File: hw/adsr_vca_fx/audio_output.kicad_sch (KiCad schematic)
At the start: 16 parts, among them J6 Conn_01x02, J7 Conn_01x02, U4 TL972, U6 TL972

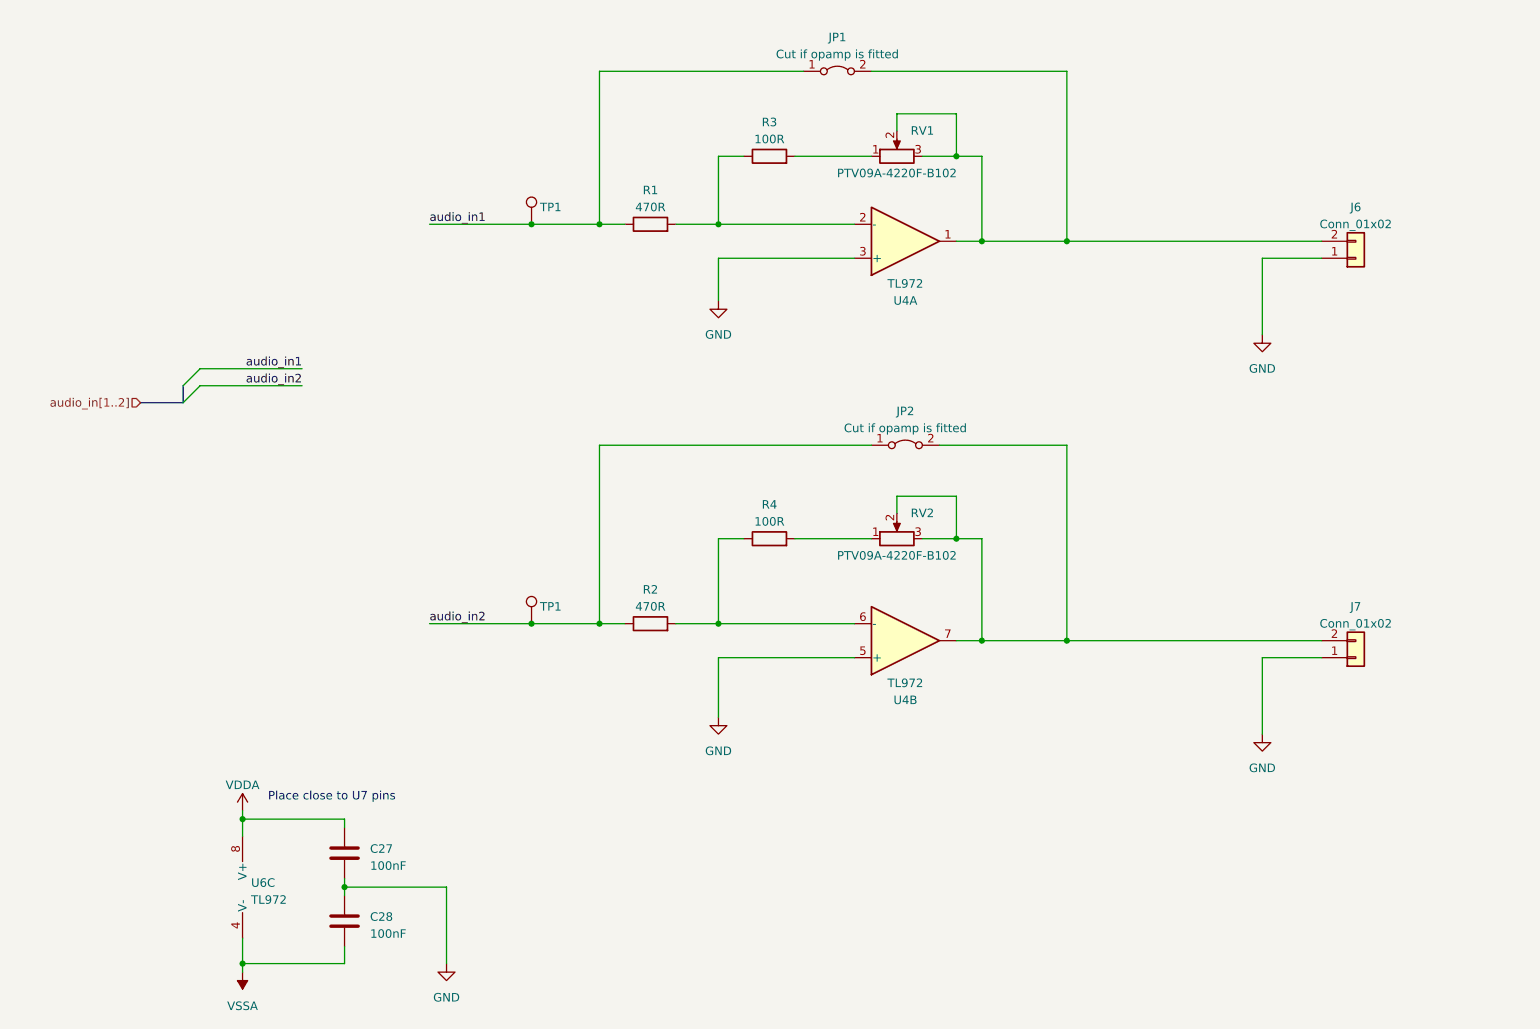
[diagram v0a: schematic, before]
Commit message: modified design into normal/inverted envlope
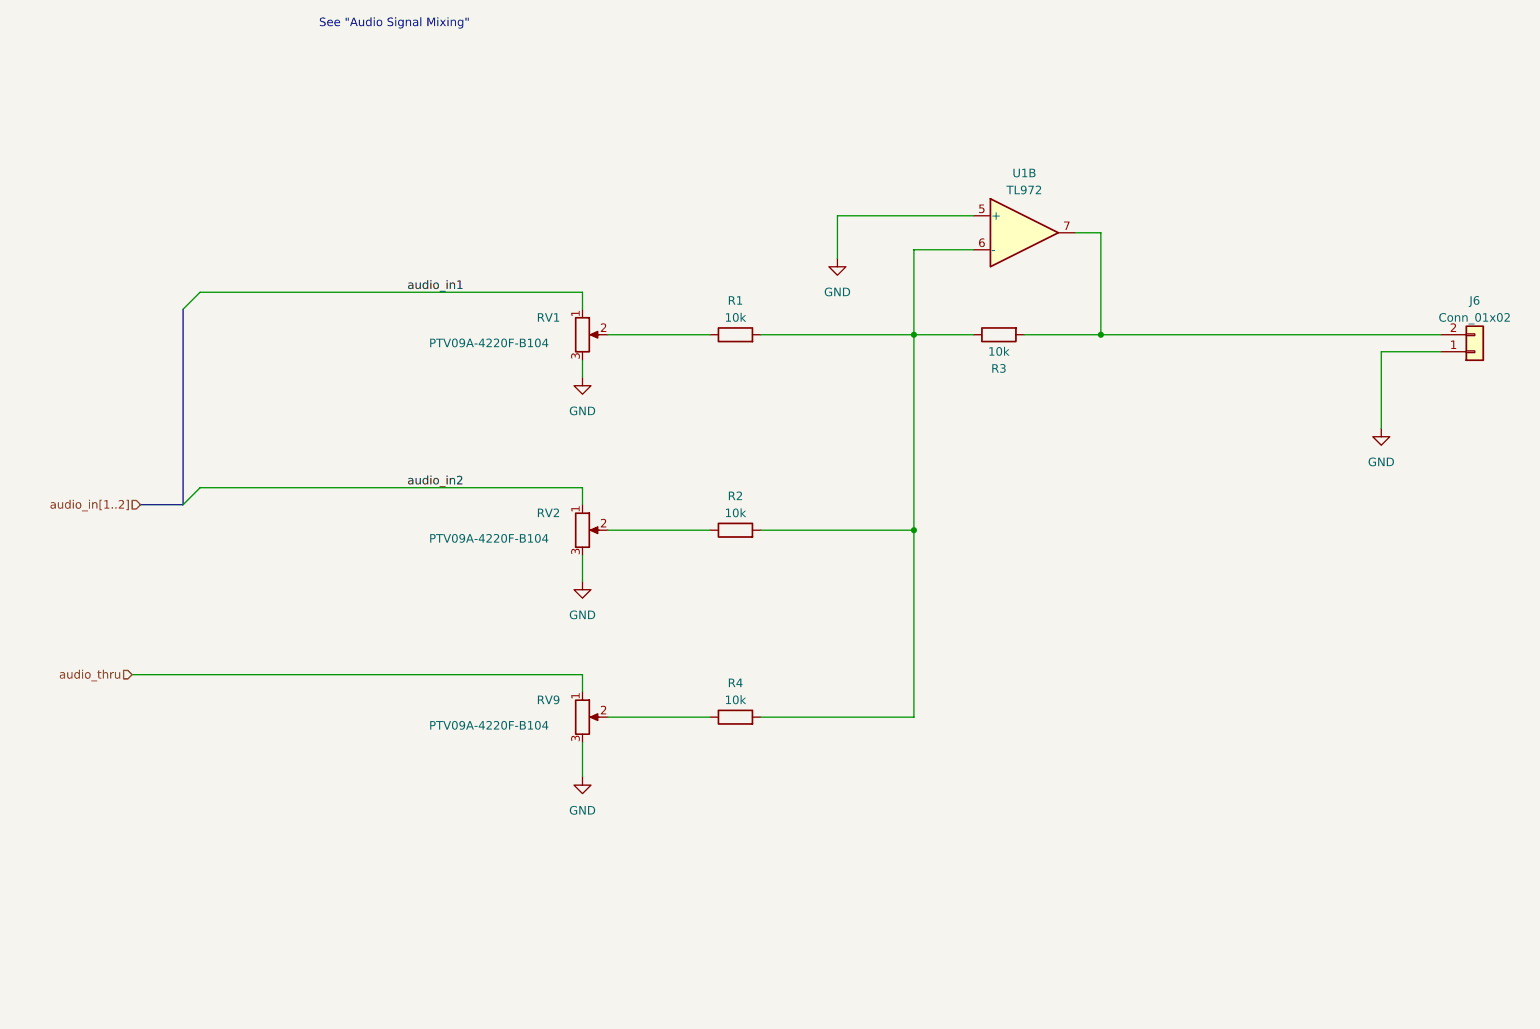
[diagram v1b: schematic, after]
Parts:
- removed C27, C28: 100nF, Capacitor_SMD:C_0805_2012Metric_Pad1.18x1.45mm_HandSolder, symbol Device:C
- removed J7: Conn_01x02, Connector_PinHeader_2.54mm:PinHeader_1x02_P2.54mm_Vertical, symbol Connector_Generic:Conn_01x02
- removed JP1, JP2: Jumper_2_Bridged, Resistor_SMD:R_0805_2012Metric_Pad1.20x1.40mm_HandSolder, symbol Jumper:Jumper_2_Bridged
- removed TP1 (x2): TestPoint, TestPoint:TestPoint_Pad_1.0x1.0mm, symbol Connector:TestPoint
- removed unit 2 of U4
- removed U6: TL972, Package_SO:SOIC-8_3.9x4.9mm_P1.27mm, symbol Amplifier_Operational:TL072
- added RV9: PTV09A-4220F-B104, Potentiometer_THT:Potentiometer_Alpha_RD901F-40-00D_Single_Vertical, symbol Device:R_Potentiometer
- R1, R2: value 470R -> 10k
- R3, R4: value 100R -> 10k
- RV1, RV2: value PTV09A-4220F-B102 -> PTV09A-4220F-B104
- renumbered U4 to U1
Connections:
- net GND: now also RV1.3, RV2.3, U1.5 (+), RV9.3; no longer U1.3 (+)
- net audio_in1: now also RV1.1; no longer R1.1
- net audio_in2: now also RV2.1; no longer R2.1
- net at RV2.2: now also R2.1; no longer RV2.3
- net at R1.2, R3.1: now also R2.2, R4.2, U1.6 (-); no longer U1.2 (-)
- net at R3.2: now also J6.2 (Pin_2), U1.7; no longer RV1.1
- net at R4.1: now also RV9.2; no longer R2.2
- new net: R1.1, RV1.2
- new net audio_thru: RV9.1
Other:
- note added: "See "Audio Signal Mixing""
- note removed: "Place close to U7 pins"
- moved on the sheet: J6, R3, RV1, U1B

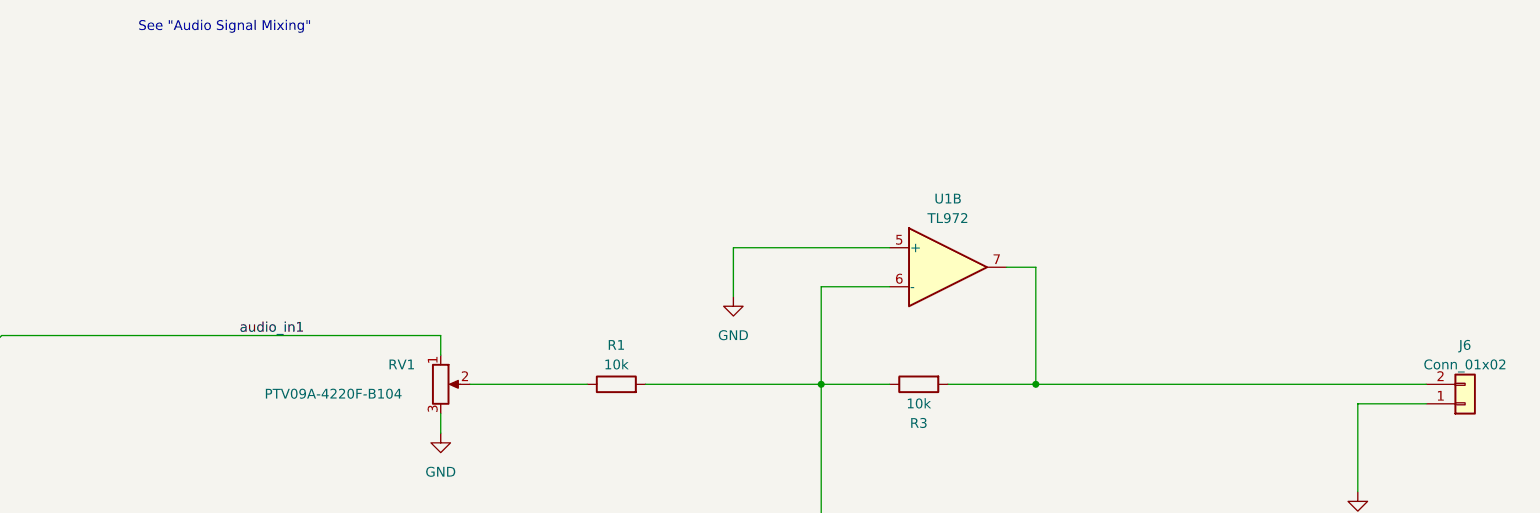
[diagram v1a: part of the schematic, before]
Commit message: updated text labels
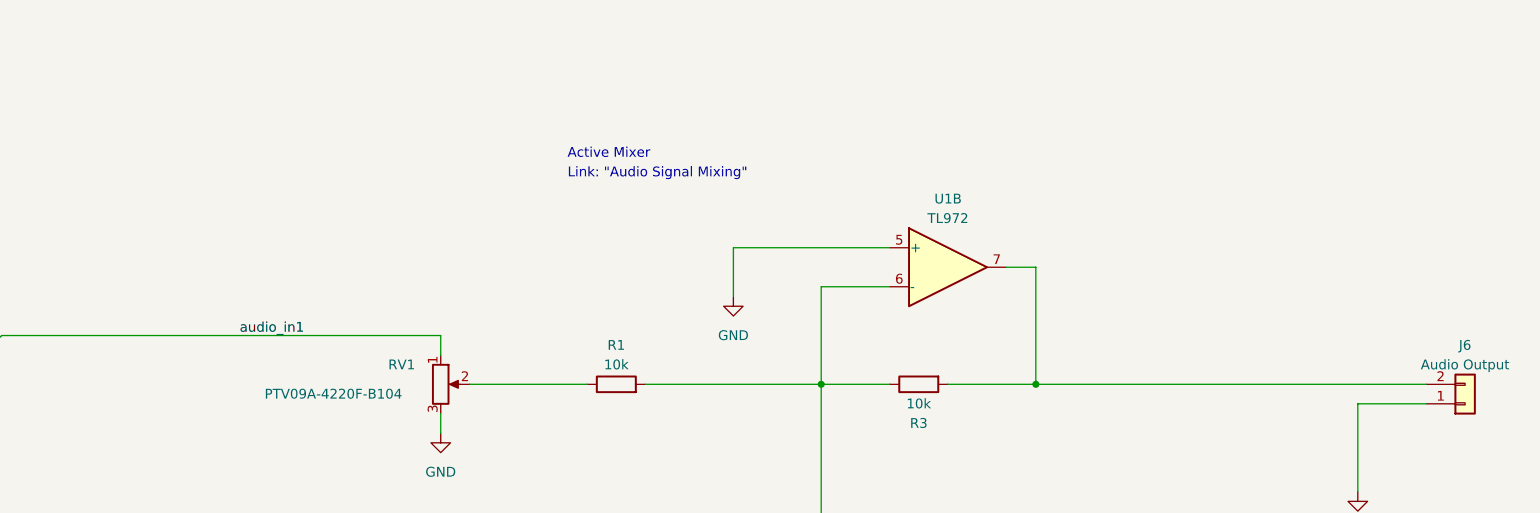
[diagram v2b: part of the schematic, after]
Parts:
- J6: value Conn_01x02 -> Audio Output
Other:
- note added: "Active Mixer"
- note added: "Link: "Audio Signal Mixing""
- note removed: "See "Audio Signal Mixing""
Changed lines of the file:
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@@
     (stroke (width 0) (type default))
   )
-  (text "See \"Audio Signal Mixing\"" (at 81.28 27.94 0)
+  (text "Link: \"Audio Signal Mixing\"" (at 137.16 46.99 0)
     (effects (font (size 1.27 1.27)) (justify left bottom) (href "https://sound-au.com/articles/audio-mixing.htm#s3"))
+  )
+  (text "Active Mixer" (at 137.16 44.45 0)
+    (effects (font (size 1.27 1.27)) (justify left bottom))
   )
   (label "audio_in1" (at 102.87 67.31 180) (fields_autoplaced)
@@
       (effects (font (size 1.27 1.27)))
     )
-    (property "Value" "Conn_01x02" (at 254 71.12 0)
-      (effects (font (size 1.27 1.27)))
-    )
+    (property "Value" "Audio Output" (at 254 71.12 0)
+      (effects (font (size 1.27 1.27)))
+    )

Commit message: first draft layout
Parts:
- renumbered J6 to J5, R1 to R2, R2 to R3, R3 to R5, RV1 to RV2, RV2 to RV3, RV9 to RV4
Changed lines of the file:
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@@
   (symbol (lib_id "Device:R") (at 143.51 102.87 90) (unit 1)
     (in_bom yes) (on_board yes) (dnp no) (fields_autoplaced)
-    (property "Reference" "R2" (at 143.51 97.79 90)
+    (property "Reference" "R3" (at 143.51 97.79 90)
       (effects (font (size 1.27 1.27)))
     )
@@
       (project "adsr_vca_fx"
         (path "/2c7cc946-dcca-4ffb-b6a0-bf0c9ddb491b/8aff0c69-c651-470d-bd06-2b6725b28795"
+          (reference "R3") (unit 1)
+        )
+      )
+    )
+  )
+  (symbol (lib_id "Device:R") (at 143.51 73.66 90) (unit 1)
+    (in_bom yes) (on_board yes) (dnp no) (fields_autoplaced)
+    (property "Reference" "R2" (at 143.51 68.58 90)
+      (effects (font (size 1.27 1.27)))
+    )
+    (property "Value" "10k" (at 143.51 71.12 90)
+      (effects (font (size 1.27 1.27)))
+    )
+    (property "Footprint" "Resistor_SMD:R_0805_2012Metric_Pad1.20x1.40mm_HandSolder" (at 143.51 75.438 90)
+      (effects (font (size 1.27 1.27)) hide)
+    )
+    (property "Datasheet" "~" (at 143.51 73.66 0)
+      (effects (font (size 1.27 1.27)) hide)
+    )
+    (pin "1")
+    (pin "2")
+    (instances
+      (project "adsr_vca_fx"
+        (path "/2c7cc946-dcca-4ffb-b6a0-bf0c9ddb491b/8aff0c69-c651-470d-bd06-2b6725b28795"
           (reference "R2") (unit 1)
-        )
-      )
-    )
-  )
-  (symbol (lib_id "Device:R") (at 143.51 73.66 90) (unit 1)
-    (in_bom yes) (on_board yes) (dnp no) (fields_autoplaced)
-    (property "Reference" "R1" (at 143.51 68.58 90)
-      (effects (font (size 1.27 1.27)))
-    )
-    (property "Value" "10k" (at 143.51 71.12 90)
-      (effects (font (size 1.27 1.27)))
-    )
-    (property "Footprint" "Resistor_SMD:R_0805_2012Metric_Pad1.20x1.40mm_HandSolder" (at 143.51 75.438 90)
-      (effects (font (size 1.27 1.27)) hide)
-    )
-    (property "Datasheet" "~" (at 143.51 73.66 0)
-      (effects (font (size 1.27 1.27)) hide)
-    )
-    (pin "1")
-    (pin "2")
-    (instances
-      (project "adsr_vca_fx"
-        (path "/2c7cc946-dcca-4ffb-b6a0-bf0c9ddb491b/8aff0c69-c651-470d-bd06-2b6725b28795"
-          (reference "R1") (unit 1)
         )
       )
@@
   (symbol (lib_id "Device:R_Potentiometer") (at 120.65 130.81 0) (unit 1)
     (in_bom yes) (on_board yes) (dnp no)
-    (property "Reference" "RV9" (at 115.57 128.27 0)
+    (property "Reference" "RV4" (at 115.57 128.27 0)
       (effects (font (size 1.27 1.27)))
     )
@@
       (project "adsr_vca_fx"
         (path "/2c7cc946-dcca-4ffb-b6a0-bf0c9ddb491b/8aff0c69-c651-470d-bd06-2b6725b28795"
-          (reference "RV9") (unit 1)
+          (reference "RV4") (unit 1)
         )
       )
@@
   (symbol (lib_id "Device:R") (at 182.88 73.66 90) (mirror x) (unit 1)
     (in_bom yes) (on_board yes) (dnp no) (fields_autoplaced)
-    (property "Reference" "R3" (at 182.88 78.74 90)
+    (property "Reference" "R5" (at 182.88 78.74 90)
       (effects (font (size 1.27 1.27)))
     )
@@
       (project "adsr_vca_fx"
         (path "/2c7cc946-dcca-4ffb-b6a0-bf0c9ddb491b/8aff0c69-c651-470d-bd06-2b6725b28795"
-          (reference "R3") (unit 1)
+          (reference "R5") (unit 1)
         )
       )
@@
   (symbol (lib_id "Device:R_Potentiometer") (at 120.65 73.66 0) (unit 1)
     (in_bom yes) (on_board yes) (dnp no)
-    (property "Reference" "RV1" (at 115.57 71.12 0)
+    (property "Reference" "RV2" (at 115.57 71.12 0)
       (effects (font (size 1.27 1.27)))
     )
@@
       (project "adsr_vca_fx"
         (path "/2c7cc946-dcca-4ffb-b6a0-bf0c9ddb491b/8aff0c69-c651-470d-bd06-2b6725b28795"
-          (reference "RV1") (unit 1)
+          (reference "RV2") (unit 1)
         )
       )
@@
   (symbol (lib_id "power:GND") (at 240.03 87.63 0) (unit 1)
     (in_bom yes) (on_board yes) (dnp no) (fields_autoplaced)
-    (property "Reference" "#PWR025" (at 240.03 93.98 0)
+    (property "Reference" "#PWR022" (at 240.03 93.98 0)
       (effects (font (size 1.27 1.27)) hide)
     )
@@
       (project "adsr_vca_fx"
         (path "/2c7cc946-dcca-4ffb-b6a0-bf0c9ddb491b/8aff0c69-c651-470d-bd06-2b6725b28795"
-          (reference "#PWR025") (unit 1)
+          (reference "#PWR022") (unit 1)
         )
       )
@@
   (symbol (lib_id "power:GND") (at 120.65 139.7 0) (unit 1)
     (in_bom yes) (on_board yes) (dnp no) (fields_autoplaced)
-    (property "Reference" "#PWR026" (at 120.65 146.05 0)
+    (property "Reference" "#PWR020" (at 120.65 146.05 0)
       (effects (font (size 1.27 1.27)) hide)
     )
@@
       (project "adsr_vca_fx"
         (path "/2c7cc946-dcca-4ffb-b6a0-bf0c9ddb491b/8aff0c69-c651-470d-bd06-2b6725b28795"
-          (reference "#PWR026") (unit 1)
+          (reference "#PWR020") (unit 1)
         )
       )
@@
   (symbol (lib_id "power:GND") (at 120.65 80.01 0) (unit 1)
     (in_bom yes) (on_board yes) (dnp no) (fields_autoplaced)
-    (property "Reference" "#PWR019" (at 120.65 86.36 0)
+    (property "Reference" "#PWR018" (at 120.65 86.36 0)
       (effects (font (size 1.27 1.27)) hide)
     )
@@
       (project "adsr_vca_fx"
         (path "/2c7cc946-dcca-4ffb-b6a0-bf0c9ddb491b/8aff0c69-c651-470d-bd06-2b6725b28795"
+          (reference "#PWR018") (unit 1)
+        )
+      )
+    )
+  )
+  (symbol (lib_id "power:GND") (at 158.75 62.23 0) (unit 1)
+    (in_bom yes) (on_board yes) (dnp no) (fields_autoplaced)
+    (property "Reference" "#PWR021" (at 158.75 68.58 0)
+      (effects (font (size 1.27 1.27)) hide)
+    )
+    (property "Value" "GND" (at 158.75 67.31 0)
+      (effects (font (size 1.27 1.27)))
+    )
+    (property "Footprint" "" (at 158.75 62.23 0)
+      (effects (font (size 1.27 1.27)) hide)
+    )
+    (property "Datasheet" "" (at 158.75 62.23 0)
+      (effects (font (size 1.27 1.27)) hide)
+    )
+    (pin "1")
+    (instances
+      (project "adsr_vca_fx"
+        (path "/2c7cc946-dcca-4ffb-b6a0-bf0c9ddb491b/8aff0c69-c651-470d-bd06-2b6725b28795"
+          (reference "#PWR021") (unit 1)
+        )
+      )
+    )
+  )
+  (symbol (lib_id "power:GND") (at 120.65 110.49 0) (unit 1)
+    (in_bom yes) (on_board yes) (dnp no) (fields_autoplaced)
+    (property "Reference" "#PWR019" (at 120.65 116.84 0)
+      (effects (font (size 1.27 1.27)) hide)
+    )
+    (property "Value" "GND" (at 120.65 115.57 0)
+      (effects (font (size 1.27 1.27)))
+    )
+    (property "Footprint" "" (at 120.65 110.49 0)
+      (effects (font (size 1.27 1.27)) hide)
+    )
+    (property "Datasheet" "" (at 120.65 110.49 0)
+      (effects (font (size 1.27 1.27)) hide)
+    )
+    (pin "1")
+    (instances
+      (project "adsr_vca_fx"
+        (path "/2c7cc946-dcca-4ffb-b6a0-bf0c9ddb491b/8aff0c69-c651-470d-bd06-2b6725b28795"
           (reference "#PWR019") (unit 1)
-        )
-      )
-    )
-  )
-  (symbol (lib_id "power:GND") (at 158.75 62.23 0) (unit 1)
-    (in_bom yes) (on_board yes) (dnp no) (fields_autoplaced)
-    (property "Reference" "#PWR023" (at 158.75 68.58 0)
-      (effects (font (size 1.27 1.27)) hide)
-    )
-    (property "Value" "GND" (at 158.75 67.31 0)
-      (effects (font (size 1.27 1.27)))
-    )
-    (property "Footprint" "" (at 158.75 62.23 0)
-      (effects (font (size 1.27 1.27)) hide)
-    )
-    (property "Datasheet" "" (at 158.75 62.23 0)
-      (effects (font (size 1.27 1.27)) hide)
-    )
-    (pin "1")
-    (instances
-      (project "adsr_vca_fx"
-        (path "/2c7cc946-dcca-4ffb-b6a0-bf0c9ddb491b/8aff0c69-c651-470d-bd06-2b6725b28795"
-          (reference "#PWR023") (unit 1)
-        )
-      )
-    )
-  )
-  (symbol (lib_id "power:GND") (at 120.65 110.49 0) (unit 1)
-    (in_bom yes) (on_board yes) (dnp no) (fields_autoplaced)
-    (property "Reference" "#PWR024" (at 120.65 116.84 0)
-      (effects (font (size 1.27 1.27)) hide)
-    )
-    (property "Value" "GND" (at 120.65 115.57 0)
-      (effects (font (size 1.27 1.27)))
-    )
-    (property "Footprint" "" (at 120.65 110.49 0)
-      (effects (font (size 1.27 1.27)) hide)
-    )
-    (property "Datasheet" "" (at 120.65 110.49 0)
-      (effects (font (size 1.27 1.27)) hide)
-    )
-    (pin "1")
-    (instances
-      (project "adsr_vca_fx"
-        (path "/2c7cc946-dcca-4ffb-b6a0-bf0c9ddb491b/8aff0c69-c651-470d-bd06-2b6725b28795"
-          (reference "#PWR024") (unit 1)
         )
       )
@@
   (symbol (lib_id "Device:R_Potentiometer") (at 120.65 102.87 0) (unit 1)
     (in_bom yes) (on_board yes) (dnp no)
-    (property "Reference" "RV2" (at 115.57 100.33 0)
+    (property "Reference" "RV3" (at 115.57 100.33 0)
       (effects (font (size 1.27 1.27)))
     )
@@
       (project "adsr_vca_fx"
         (path "/2c7cc946-dcca-4ffb-b6a0-bf0c9ddb491b/8aff0c69-c651-470d-bd06-2b6725b28795"
-          (reference "RV2") (unit 1)
+          (reference "RV3") (unit 1)
         )
       )
@@
   (symbol (lib_id "Connector_Generic:Conn_01x02") (at 254 76.2 0) (mirror x) (unit 1)
     (in_bom yes) (on_board yes) (dnp no) (fields_autoplaced)
-    (property "Reference" "J6" (at 254 68.58 0)
+    (property "Reference" "J5" (at 254 68.58 0)
       (effects (font (size 1.27 1.27)))
     )
@@
       (project "adsr_vca_fx"
         (path "/2c7cc946-dcca-4ffb-b6a0-bf0c9ddb491b/8aff0c69-c651-470d-bd06-2b6725b28795"
-          (reference "J6") (unit 1)
-        )
-      )
+          (reference "J5") (unit 1)
+        )
+      )
